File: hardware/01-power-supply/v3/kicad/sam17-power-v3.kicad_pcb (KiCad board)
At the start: 2 copper layers, 200 x 150 mm, 113 parts, among them J1 Barrier block 3 pos, J2 Molex KK-254 4 pos, J3 Barrier block 3 pos, J4 Barrier block 2 pos, J5 Vogt 3866A.68 faston 6.3x0.8 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, J6 Molex KK-254 2 pos, J7 Barrier block 2 pos, J8 JST-PH 4 pos, U1 LM2941CT/NOPB, U10 ADS1115IDGSR — ADC 16 bits 4 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, U11 TMP1075DGKR — sensor de tempe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, U12 ISO1541D — aislador I2C bidir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, U2 LM2991T/NOPB, U3 LM7805, U4 LT3045EDD#TRPBF, U5 LT3045EDD#TRPBF, U6 LT3094EDD#PBF, U7 LT3094EDD#PBF, U8 INA226AIDGSR — monitor I/V I2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, U9 INA226AIDGSR — monitor I/V I2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

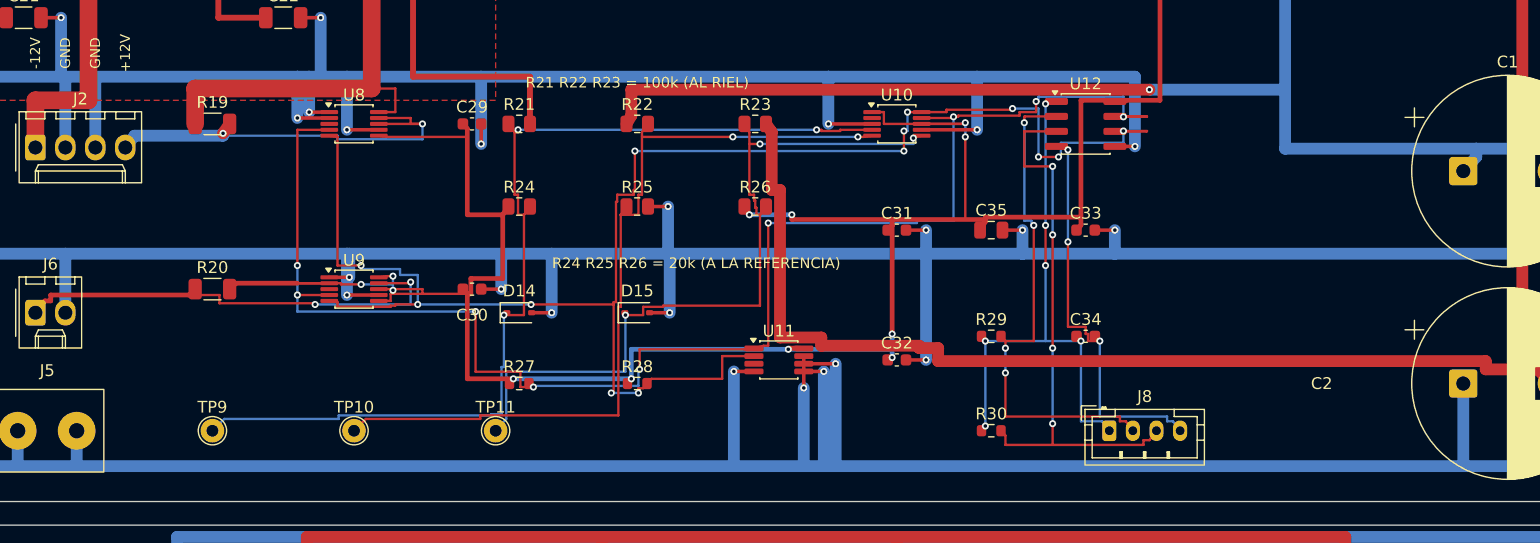
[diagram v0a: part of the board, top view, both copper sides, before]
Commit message: El arbol de masa vuelve a ser un arbol: la puerta mira las vias, y sobraban dos
La puerta del PCB dejo de regenerar el ruteo (#139) y con ello gano medir el
artefacto, pero la regla de la estrella cambio la identidad de su nodo: paso de
una coordenada a una coordenada MAS la capa, y nunca miro la lista de vias. Con
eso, una espira que sale por una cara y vuelve por la otra dejaba de verse. En
una placa de dos capas con masa en las dos y 38 transiciones de capa, esa es LA
forma en que un lazo aparece, y es la que sec.7 prohibe por ser una espira de
100 Hz acoplada a todo.

Y no era teorico. Con las vias en el grafo, el cobre commiteado tenia DOS
espiras: tres pads de GND de U11 comparten su rabito en F.Cu -- uno cruza por
encima de los otros dos -- y cada uno bajaba con su propia via a la misma
costilla. Sobraban dos bajadas.

La regla, en grafo_gnd():

- el nodo sigue siendo (x, y, capa): dos cobres que se cruzan en capas
  distintas NO son un nodo, y unirlos inventaria bucles que no existen;
- cada via de la red con cobre en sus dos caras aporta una arista, que es por
  donde la espira se cerraba;
- los tramos se parten tambien en las vias, no solo en los cruces: una via a
  mitad de pista une igual, y sin partir ahi no hay nodo que unir. Lo destapo
  un canario, no una lectura;
- los nodos se agrupan con 1 um de tolerancia en vez de redondearse. Redondear
  puede separar mas: dos puntos a media micra caen a los dos lados de la
  frontera. El generador escribia los enganches a 3 decimales y las vias en
  cuartos de mil, y ese desfase partia el nodo justo donde pasaba el lazo.

La placa, en el generador: se podan las vias que cierran ciclo. Quitar una
arista que cierra un ciclo no desconecta nunca, asi que el ratsnest sigue en
cero. Al quitarlas se quedaba colgando su bajante y su rabito, cuatro tramos
que el DRC canta como track_dangling, y se recortan por tramos -- el rabito
vertical de U11 sujeta tres pads en su primera mitad y solo sobra la segunda.
Eso sube a r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
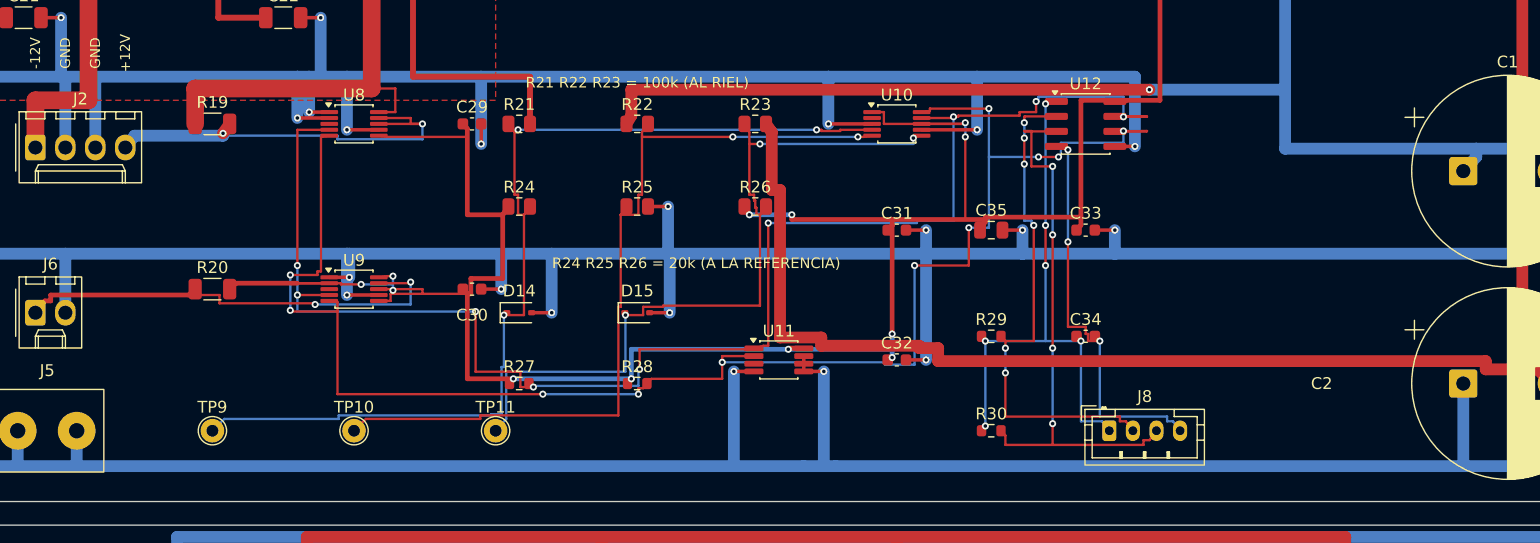
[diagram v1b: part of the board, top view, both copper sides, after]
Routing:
- net GND: track 1488.7 -> 1469.3 mm, vias 42 -> 40
- net /SCL_A: track 141.1 -> 137.5 mm, vias 13 -> 11
- net /SDA_D: vias 4 -> 6

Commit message: La corriente de rectificacion dejo de dar la vuelta a la placa: 57,49 -> 2,44 cm2
El guion del zumbido medía la v1, que no se construye (#280). Apuntarlo a la v3
era la mitad del arreglo; la otra mitad era el metodo.

Medía una CAJA ENVOLVENTE alrededor de J1, BR1, C1 y C12. Un rectangulo
alrededor de cuatro piezas mide lo mismo se vaya el retorno por donde se vaya, y
lo que acopla es el area que ENCIERRA el camino. Ahora traza el cobre: sigue el
recorrido electrico de verdad -- con las vias y los pads pasantes en el grafo,
que es por donde VRAW+ cambia de capa aqui sin ninguna via -- y firma el area
con la formula del cordon de zapato. Firmarla importa: un camino que va y vuelve
sobre si mismo gasta cobre y no encierra flujo.

Con eso, la v3 daba 57,49 cm2. No era un lazo mal dibujado: era el arbol de
masa. J1.2 -- la toma central del secundario, por donde vuelve TODA la corriente
de rectificacion, 2,5 A en picos con flancos de microsegundos, la mas grande de
la placa -- caia por cercania en la costilla de y=66, y los dos bulk en la de
y=99. Las dos costillas solo se tocan por el tronco en x=11, asi que cada pico
se iba 379 mm hasta el canto izquierdo de la placa y volvia.

El propio generador ya declaraba la intencion correcta: "raiz electrica en J1.2,
la toma central del secundario -- que es por donde vuelve la corriente de
rectificacion". El reparto por cercania no la cumplia. Nombrar un nodo raiz no
acorta su camino: en un arbol la raiz es una etiqueta, lo que cuenta es por
donde va el cobre entre los dos puntos que llevan la corriente.

GND_COSTILLA_FORZADA pone J1.2 en la costilla de los bulk. Sigue siendo un
arbol: J1.2 cambia de rama, no gana una segunda. Y de paso el pico de
rectificacion sale del tronco y de la costilla de y=99, asi que baja tambien la
impedancia que comparte con todo lo que cuelga de ellos.

                        vuelta de masa      area encerrada   inducido a 150 mm
  v1 trazada             60 / 102 mm          3,90 cm2               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
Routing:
- net GND: track 1469.3 -> 1414.8 mm
- net /VRAW+: track 333.0 -> 325.8 mm, vias 8 -> 6
